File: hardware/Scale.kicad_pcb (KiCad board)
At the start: 2 copper layers, 45 x 45 mm, 109 parts, among them J1 Load Cell Connector, J2 GPIO, J3 RS232, J4 DebugEdge_02x03, J5 Display Connector, J7 12401610E4#2A, Q1 DMG2307L, Q2 DMG2307L, Q3 BSD235N, SW1 RESET, U1 STM32G070CBTx_u, U10 MCP6001-OT, U2 MCP3562R-E/ST, U3 MCP6N11-010, U4 MCP4542, U7 AP9101CK, U8 MIC5504-3.3YM5, U9 MCP6001-OT, X1 KC2520Z

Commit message: Added labels
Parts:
- added kibuzzard-692359F1: G***, kibuzzard-692359F1, B.Cu at (119.8, 61.6)
- added kibuzzard-69235A05: G***, kibuzzard-69235A05, B.Cu at (119.8, 63.6)
- added kibuzzard-69235A0F: G***, kibuzzard-69235A0F, B.Cu at (119.8, 65.7)
- added kibuzzard-69235A65: G***, kibuzzard-69235A65, F.Cu at (119.8, 61.6)
- added kibuzzard-69235A78: G***, kibuzzard-69235A78, F.Cu at (119.8, 63.6)
- added kibuzzard-69235A81: G***, kibuzzard-69235A81, F.Cu at (119.8, 65.7)
- added kibuzzard-69235C19: G***, kibuzzard-69235C19, B.Cu at (156.4, 50.9)
- added kibuzzard-69235C25: G***, kibuzzard-69235C25, B.Cu at (155.2, 50.9)
- added kibuzzard-69235C2C: G***, kibuzzard-69235C2C, B.Cu at (153.9, 50.9)
- added kibuzzard-69235C31: G***, kibuzzard-69235C31, B.Cu at (156.4, 58.6)
- added kibuzzard-69235C3D: G***, kibuzzard-69235C3D, B.Cu at (155.2, 58.6)
- added kibuzzard-69235C43: G***, kibuzzard-69235C43, B.Cu at (153.9, 58.6)
- added kibuzzard-69235C86: G***, kibuzzard-69235C86, B.Cu at (149.9, 59.0)
- added kibuzzard-69235CAB: G***, kibuzzard-69235CAB, B.Cu at (151.9, 54.9)
- added kibuzzard-69235CD0: G***, kibuzzard-69235CD0, B.Cu at (151.6, 65.0)
- added kibuzzard-69235CE7: G***, kibuzzard-69235CE7, B.Cu at (149.9, 70.3)
- added kibuzzard-69235D1A: G***, kibuzzard-69235D1A, B.Cu at (142.6, 69.5)
- added kibuzzard-69235D2C: G***, kibuzzard-69235D2C, B.Cu at (134.1, 63.5)
- added kibuzzard-69235D46: G***, kibuzzard-69235D46, B.Cu at (134.3, 56.1)
- added kibuzzard-69235D61: G***, kibuzzard-69235D61, B.Cu at (131.8, 56.0)
- added kibuzzard-69235D70: G***, kibuzzard-69235D70, B.Cu at (133.1, 49.8)
- added kibuzzard-69235D7B: G***, kibuzzard-69235D7B, B.Cu at (135.7, 49.8)
- added kibuzzard-69235D86: G***, kibuzzard-69235D86, B.Cu at (138.3, 49.8)
- added kibuzzard-69235DBF: G***, kibuzzard-69235DBF, B.Cu at (150.0, 51.5)
- added kibuzzard-69235DD0: G***, kibuzzard-69235DD0, B.Cu at (147.5, 51.6)
- added kibuzzard-69235DDD: G***, kibuzzard-69235DDD, B.Cu at (144.9, 51.6)
- added kibuzzard-69235DE8: G***, kibuzzard-69235DE8, B.Cu at (142.4, 51.5)
- added kibuzzard-69235E07: G***, kibuzzard-69235E07, B.Cu at (117.8, 69.9)
- added kibuzzard-69235E1A: G***, kibuzzard-69235E1A, B.Cu at (117.7, 72.4)
- added kibuzzard-69235E34: G***, kibuzzard-69235E34, B.Cu at (117.7, 75.0)
- added kibuzzard-69235E43: G***, kibuzzard-69235E43, B.Cu at (117.8, 77.5)
- added kibuzzard-69235E53: G***, kibuzzard-69235E53, B.Cu at (117.7, 80.1)
- added kibuzzard-69235E66: G***, kibuzzard-69235E66, B.Cu at (117.1, 87.0)
- added kibuzzard-69235E74: G***, kibuzzard-69235E74, B.Cu at (119.6, 87.0)
- added kibuzzard-69235E84: G***, kibuzzard-69235E84, B.Cu at (122.2, 87.0)
- added kibuzzard-69235EA0: G***, kibuzzard-69235EA0, B.Cu at (124.7, 87.0)
- added kibuzzard-69235EC4: G***, kibuzzard-69235EC4, B.Cu at (127.3, 87.0)
- added kibuzzard-69235ED0: G***, kibuzzard-69235ED0, B.Cu at (129.8, 87.0)
- added kibuzzard-69235EDC: G***, kibuzzard-69235EDC, B.Cu at (132.3, 87.0)
- added kibuzzard-69235EE8: G***, kibuzzard-69235EE8, B.Cu at (134.9, 87.0)
- added kibuzzard-69235EF4: G***, kibuzzard-69235EF4, B.Cu at (137.4, 87.0)
- added kibuzzard-69235F49: G***, kibuzzard-69235F49, B.Cu at (117.8, 82.6)
- added kibuzzard-69235FA0: G***, kibuzzard-69235FA0, B.Cu at (122.6, 64.4)
- added kibuzzard-69235FE1: G***, kibuzzard-69235FE1, B.Cu at (120.3, 80.7)
- added kibuzzard-69236006: G***, kibuzzard-69236006, B.Cu at (136.7, 84.5)
- added kibuzzard-69236027: G***, kibuzzard-69236027, B.Cu at (125.2, 84.4)
- added kibuzzard-69236067: G***, kibuzzard-69236067, B.Cu at (144.8, 54.1)
- added kibuzzard-692360F1: G***, kibuzzard-692360F1, B.Cu at (127.3, 62.8)
- added kibuzzard-69236118: G***, kibuzzard-69236118, B.Cu at (131.7, 62.8)
- moved TP5 1.71 mm to (151.9, 52.9)
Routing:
- net Net-(R5-Pad2): track 0.00 -> 1.84 mm

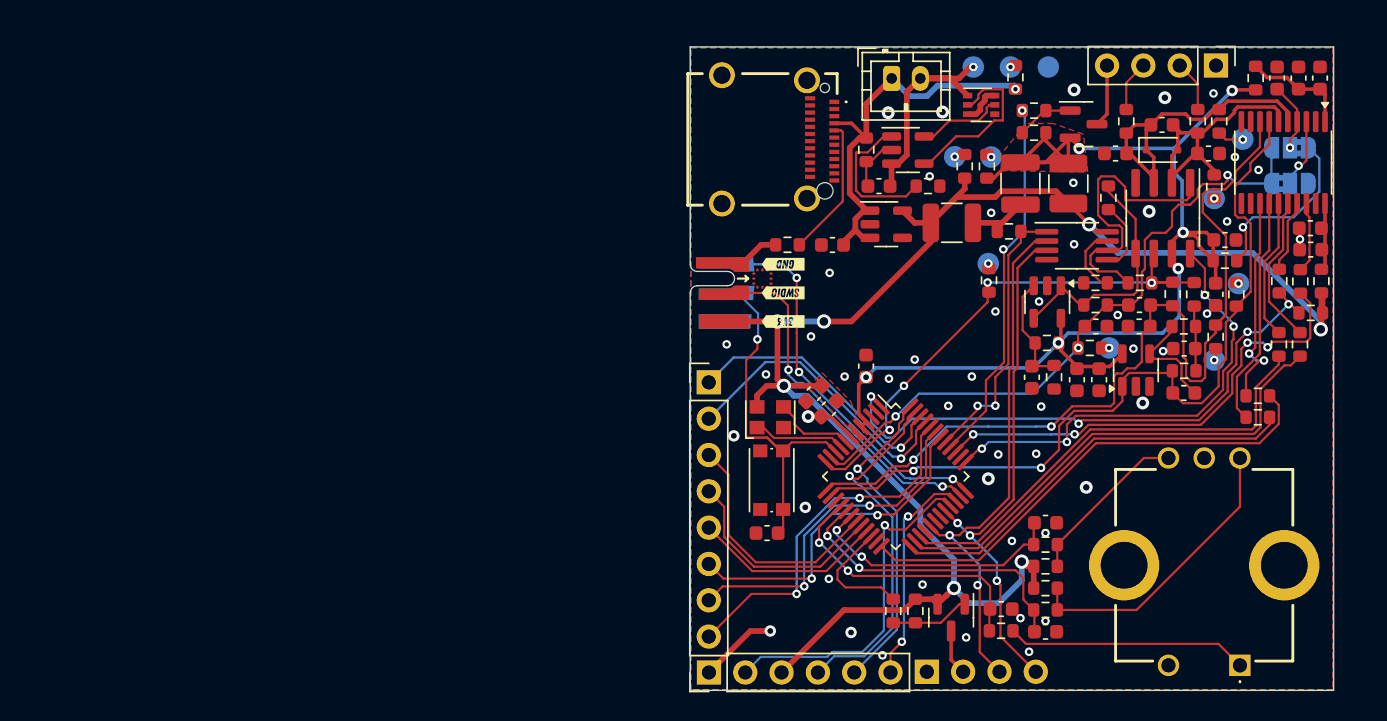
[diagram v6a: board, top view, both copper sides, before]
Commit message: Rearrange labels
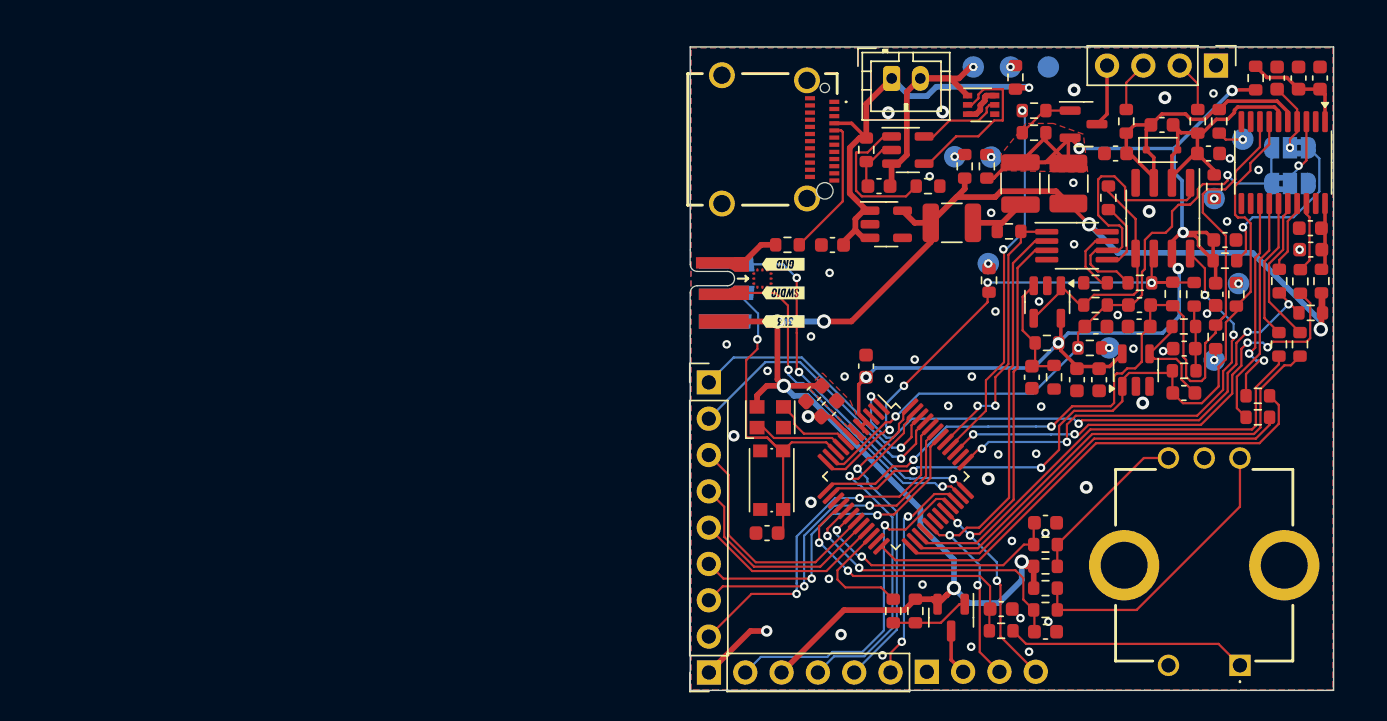
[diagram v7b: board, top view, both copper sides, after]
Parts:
- moved kibuzzard-69235DBF 0.65 mm to (150.0, 50.9)
- moved kibuzzard-69235DD0 0.65 mm to (147.5, 50.9)
- moved kibuzzard-69235DE8 0.65 mm to (142.4, 50.9)
- moved kibuzzard-69235DDD 0.65 mm to (144.9, 50.9)
- moved kibuzzard-69236067 0.55 mm to (144.8, 53.5)
- moved kibuzzard-69235CD0 0.15 mm to (151.6, 64.8)
- moved kibuzzard-69235D1A 0.15 mm to (142.6, 69.3)
- moved kibuzzard-69235C86 0.15 mm to (149.9, 58.9)
- moved kibuzzard-69235CAB 0.15 mm to (151.9, 54.7)
- moved kibuzzard-69235D2C 0.15 mm to (134.1, 63.4)
- moved kibuzzard-69235D46 0.15 mm to (134.3, 56.0)
- moved kibuzzard-69235D61 0.15 mm to (131.8, 55.9)
- moved kibuzzard-69235CE7 0.15 mm to (149.9, 70.2)
- moved kibuzzard-69235D70 0.10 mm to (133.1, 49.6)
- moved kibuzzard-69235D7B 0.10 mm to (135.7, 49.6)
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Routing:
- net +BATT: track 27.6 -> 29.3 mm

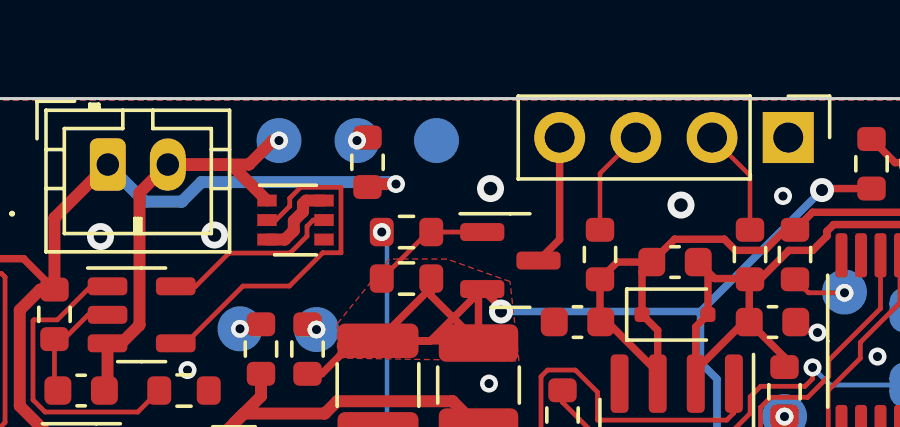
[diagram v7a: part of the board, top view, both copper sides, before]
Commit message: Added test point
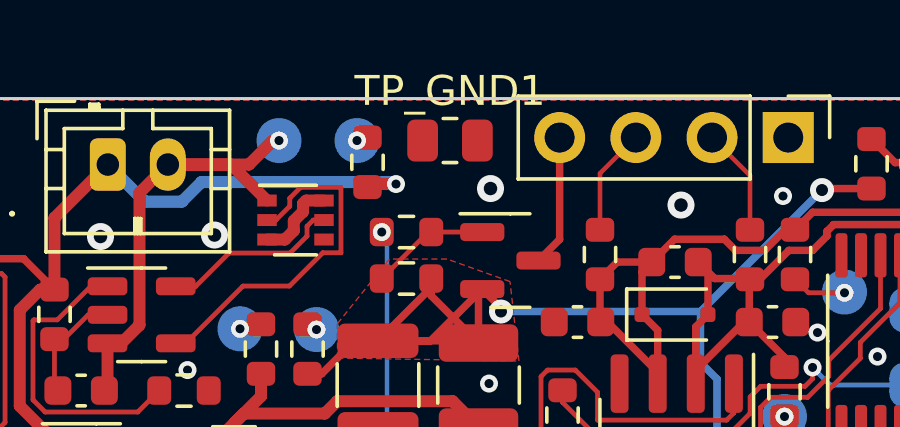
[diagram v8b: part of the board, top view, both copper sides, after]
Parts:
- TP_GND1: footprint TestPoint:TestPoint_Pad_D1.5mm -> Resistor_SMD:R_0805_2012Metric; moved to F.Cu
- moved TP_GND1 0.45 mm to (138.8, 47.9), turned to 0 degrees
